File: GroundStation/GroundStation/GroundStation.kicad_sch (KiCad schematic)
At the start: 26 parts, among them J1 SD_Card_Receptacle, P1 USB_C_Plug_USB2.0, U1 STM32F103C8Tx, U4 NEO-M9N

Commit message: add little
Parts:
- renumbered R1_down to R1_up
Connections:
- net 3v3: now also R1_up.1
- net GND: no longer R1_up.2
- net USART1_GPS_EXT: now reaches U1.45 (PB8)
- net PB11_MCU_DOut: now reaches U4.8 (~{RESET})
- net PB10_DigitalOutput_whenHigh_ChipWork: no longer names the net of U4.2 (D_SEL)
- net PB10_DigitalOutput_whenHigh_ChipWork: now also R1_up.2; no longer R1_up.1
- net USART1_GPS_D_SEL renamed USART1_GPS_RESET
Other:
- note added: "Let GPS always work"
- note added: "high-gain Antenna + auto tracking 920HZ"
- note added: "low-gain Omni Antenna 433HZ"
- moved on the sheet: AE1, AE2, C1, C10, C3, C4, C5, C6, C7, C8, C9, D1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

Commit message: GPS_Ground Revise
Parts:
- added C39: 10u, symbol Device:C
- added C40: 100n, symbol Device:C
- added C41: NC, symbol Device:C
- added C42: 100p, symbol Device:C
- added D4: GPS_LED, symbol Device:LED
- added J4: Conn_Coaxial, symbol Connector:Conn_Coaxial
- added L2: short, symbol Device:L
- added R26: 1k, symbol Device:R
- added R27: NC, symbol Device:R
- added R29: 10k, symbol Device:R
- added TP1: GPS_BOOT, symbol Connector:TestPoint
- added U9: NEO-M9N-00B, SMT_9N-00B_UBL, symbol A_library:NEO-M9N-00B
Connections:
- net I_dont_know_if _it_CS?PA8 is gone; now on net SPI1_LoRa2_SCK: UE80-900M2213S.p6 (NSS)
- net PA11_USB_DX is gone; now on net USB_DX_D-: P1.A7 (D-)
- net PA12_USB_DP is gone; now on net USB_DP_D+: P1.A6 (D+)
- net PA2_TX_MCU is gone; now on net VCC: U2. (M1)
- net PA3_RX_MCU is gone; now on net VCC: U2. (M1)
- net PA4 is gone; now on net VCC: U2. (M1)
- net PA5 is gone; now on net SPI1_LoRa2_SCK: UE80-900M2213S.p6 (NSS)
- net PA6 is gone; now on net SPI1_LoRa2_MISO: UE80-900M2213S.p3 (MISO)
- net PA7 is gone; now on net SPI1_LoRa2_MOSI: UE80-900M2213S.p4 (MOSI)
- net PB1 is gone; now on net VCC: U2. (M1)
- net PB10_CS is gone; now on net SPI2_SDcard_CS: J1.1 (CD/DAT3), R2_up.2
- net PB13_SCK is gone; now on net SPI2_SDcard_MOSI: J1.5 (CLK)
- net PB14_MISO is gone; now on net SPI2_SDcard_MISO: J1.7 (DAT0)
- net PB15_MOSI is gone; now on net SPI2_SDcard_SCK: J1.2 (CMD)
- net PB2 is gone; now on net VCC: U2. (M1)
- net +3.3V: now also C39.1, C40.1, R29.1, U9.22 (V_BCKP), U9.23 (VCC)
- net GND: now also C39.2, C40.2, C41.2, D4.1 (K), J4.2 (Ext), U9.10 (GND), U9.12 (GND), U9.13 (GND), U9.24 (GND)
- net SPI1_LoRa2_CS: now also UE80-900M2213S.p6 (NSS)
- net USART1_GPS_RESET: now also R29.2, U9.8 (RESET_N)
- net USART1_GPS_RX: now also U9.20 (TXD_/_SPI_MISO)
- net USART1_GPS_TX: now also U9.21 (RXD_/_SPI_MOSI)
- net USART2_LoRa1_AUX: now also U2. (M1)
- net USART2_LoRa1_M0: now also U2. (M1)
- net USART2_LoRa1_M1: now also U2. (M1)
- net USART2_LoRa1_NRST: now also C5.1, R3_up.2, U2. (M1)
- net USART2_LoRa1_RX: now also U2. (M1)
- net USART2_LoRa1_TX: now also U2. (M1)
- removed net PB0: C5.1, R3_up.2, U2. (M1)
- net USART1_GPS_EXT: no longer names the net of U1.45 (PB8)
- new net: C41.1, C42.1, L2.2, R27.1
- new net: J4.1 (In), L2.1
- new net: D4.2 (A), R26.1
- new net: C42.2, U9.11 (RF_IN)
- new net: TP1.1, U9.1 (SAFEBOOT_N)
- new net: R26.2, U9.3 (TIMEPULSE)
- new net: R27.2, U9.9 (VCC_RF)
- no-connect marks 5 -> 16
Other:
- note added: "MCU的TX跟RX"
- note added: "Reserved for active atenna"
- moved on the sheet: AE1, AE2, C1, C10, C3, C4, C5, C6, C7, C8, C9, D1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

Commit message: Ray start GroundStation PCB
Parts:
- removed C1: 0.1uF, symbol Device:C
- removed R1_up: 10k, symbol Device:R
- removed U4: NEO-M9N, RF_GPS:ublox_NEO, symbol RF_GPS:NEO-M9N
- added C21, C23: 100n, Capacitor_SMD:C_0805_2012Metric_Pad1.18x1.45mm_HandSolder, symbol Device:C
- added C22, C24: 47u, Capacitor_SMD:C_0805_2012Metric_Pad1.18x1.45mm_HandSolder, symbol Device:C
- added D2: G_5V, LED_SMD:LED_0805_2012Metric_Pad1.15x1.40mm_HandSolder, symbol Device:LED
- added D3: B_3V3, LED_SMD:LED_0805_2012Metric_Pad1.15x1.40mm_HandSolder, symbol Device:LED
- added R16, R17: 1k, Resistor_SMD:R_0805_2012Metric, symbol Device:R
- added U3: LD1117S33TR_SOT223, Package_TO_SOT_SMD:SOT-223-3_TabPin2, symbol Regulator_Linear:LD1117S33TR_SOT223
- AE1, AE2: footprint (none) -> Connector_Coaxial:SMA_Molex_73251-1153_EdgeMount_Horizontal
- C10, C2, C3, C39, C4, C40, C41, C42, C5, C6, C7, C8, C9: footprint (none) -> Capacitor_SMD:C_0805_2012Metric_Pad1.18x1.45mm_HandSolder
- C66: renamed from C6; footprint (none) -> Capacitor_SMD:C_0805_2012Metric_Pad1.18x1.45mm_HandSolder
- C77: renamed from C7; footprint (none) -> Capacitor_SMD:C_0805_2012Metric_Pad1.18x1.45mm_HandSolder
- D4: footprint (none) -> LED_SMD:LED_0805_2012Metric_Pad1.15x1.40mm_HandSolder
- FB1: footprint (none) -> Inductor_SMD:L_2512_6332Metric
- J1: footprint (none) -> Connector_Card:SD_Kyocera_145638109511859+
- J4: footprint (none) -> Connector_Coaxial:BNC_Amphenol_B6252HB-NPP3G-50_Horizontal
- L2: footprint (none) -> Inductor_SMD:L_Bourns_SDR0604
- P1: footprint (none) -> Connector_USB:USB3_A_Molex_48393-001
- R26, R27, R29, R3_up1: footprint (none) -> Resistor_SMD:R_0805_2012Metric
- R2_up1: renamed from R2_up; footprint (none) -> Resistor_SMD:R_0805_2012Metric
- R3_up2: renamed from R3_up; footprint (none) -> Resistor_SMD:R_0805_2012Metric
- TP1: footprint (none) -> TestPoint:TestPoint_Pad_D1.0mm
- U2: value ~ -> E22-400T30S_LoRa
- U9: footprint SMT_9N-00B_UBL -> RF_GPS:ublox_NEO
- renumbered UE80-900M2213S to UE80-900M2213S1
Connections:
- net 3v3 is gone; now on net 3.3V: C2.1, J1.4 (VDD), R2_up1.1
- net +5V: now also C23.1, R16.2, U3.3 (VI)
- net GND: now also C21.2, C22.2, C23.2, C24.2, D2.1 (K), D3.1 (K), U3.1 (GND)
- net SPI1_LoRa2_CS: now also UE80-900M2213S1.p7 (NSS); no longer UE80-900M2213S1.p6 (NSS)
- net +3.3V renamed 3.3V
- net 3.3V: now also C3.1, C4.1, R3_up2.1, U2. (M1), C21.1, C22.1, C24.1, R17.2, U3.2 (VO)
- removed net VCC: C3.1, C4.1, R3_up2.1, U2. (M1)
- new net: D2.2 (A), R16.1
- new net: D3.2 (A), R17.1
- no-connect marks 16 -> 41
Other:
- note added: "Indicator"
- note added: "LDO"
- note removed: "Let GPS always work"
- moved on the sheet: C10, C6, C66, C7, C77, C8, C9, FB1, TP1, U1

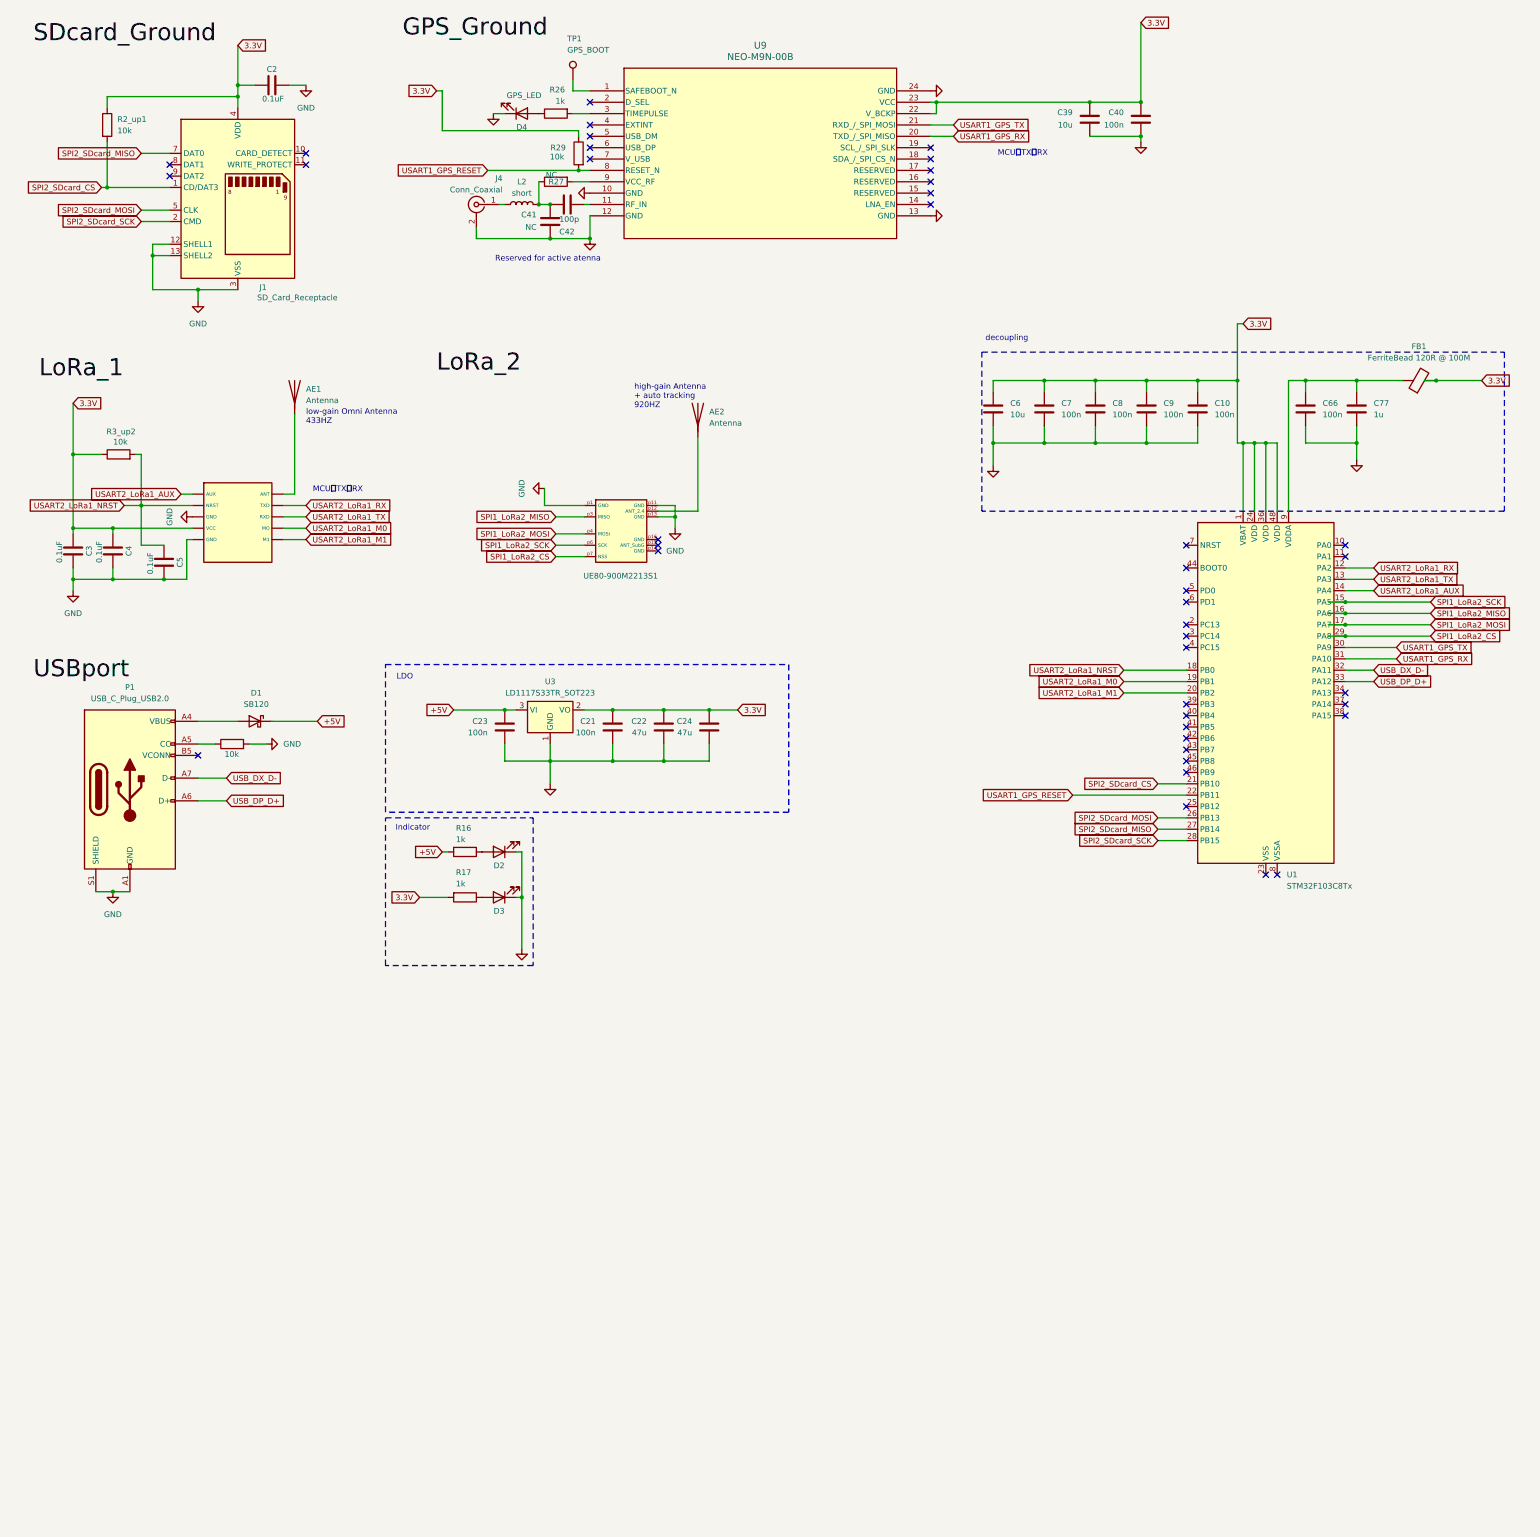
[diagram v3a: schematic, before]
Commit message: assign package for groundstation
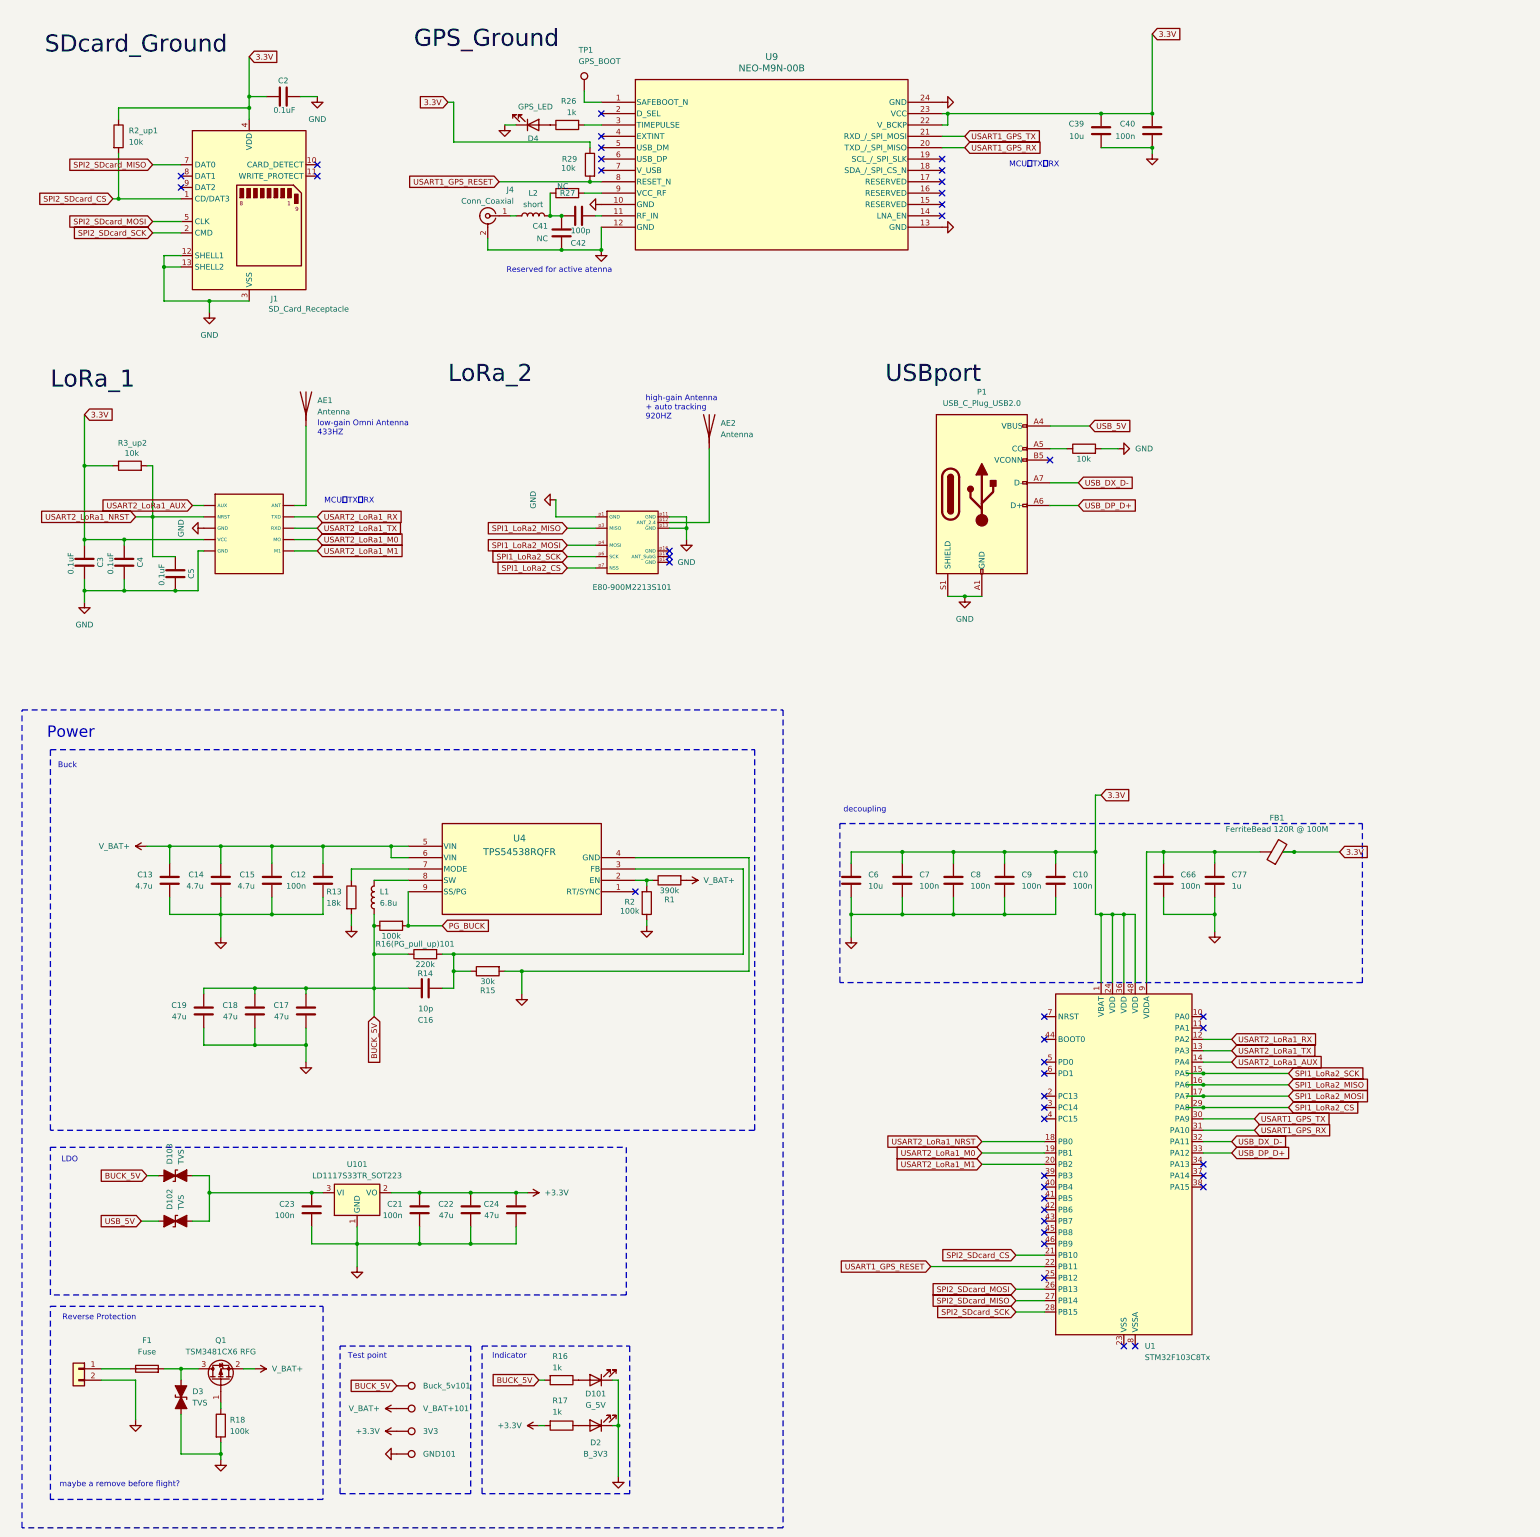
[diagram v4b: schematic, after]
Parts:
- removed D1: SB120, Diode_THT:D_DO-41_SOD81_P10.16mm_Horizontal, symbol Diode:SB120
- removed D2: G_5V, LED_SMD:LED_0805_2012Metric_Pad1.15x1.40mm_HandSolder, symbol Device:LED
- removed U3: LD1117S33TR_SOT223, Package_TO_SOT_SMD:SOT-223-3_TabPin2, symbol Regulator_Linear:LD1117S33TR_SOT223
- added 3V3, Buck_5v101, GND101, V_BAT+101: TestPoint, TestPoint:TestPoint_Pad_2.0x2.0mm, symbol Connector:TestPoint
- added C12: 100n, Capacitor_SMD:C_0805_2012Metric_Pad1.18x1.45mm_HandSolder, symbol Device:C
- added C13, C14, C15: 4.7u, Capacitor_SMD:C_0805_2012Metric_Pad1.18x1.45mm_HandSolder, symbol Device:C
- added C16: 10p, Capacitor_SMD:C_0805_2012Metric_Pad1.18x1.45mm_HandSolder, symbol Device:C
- added C17, C18, C19: 47u, Capacitor_SMD:C_0805_2012Metric_Pad1.18x1.45mm_HandSolder, symbol Device:C
- added D101: G_5V, LED_SMD:LED_0805_2012Metric_Pad1.15x1.40mm_HandSolder, symbol Device:LED
- added D102, D103, D3: TVS, Diode_SMD:D_SOD-123, symbol Device:D_TVS_Filled
- added F1: Fuse, Fuse:Fuse_1206_3216Metric, symbol Device:Fuse
- added J5: Conn_01x02, Connector_PinHeader_2.54mm:PinHeader_1x02_P2.54mm_Horizontal, symbol Connector_Generic:Conn_01x02
- added L1: 6.8u, Inductor_SMD:L_0805_2012Metric_Pad1.05x1.20mm_HandSolder, symbol Device:L
- added Q1: TSM3481CX6 RFG, Package_TO_SOT_SMD:SOT-23, symbol Transistor_FET:IRLML6402
- added R1: 390k, Resistor_SMD:R_0805_2012Metric_Pad1.20x1.40mm_HandSolder, symbol Device:R
- added R13: 18k, Resistor_SMD:R_0805_2012Metric_Pad1.20x1.40mm_HandSolder, symbol Device:R
- added R14: 220k, Resistor_SMD:R_0805_2012Metric_Pad1.20x1.40mm_HandSolder, symbol Device:R
- added R15: 30k, Resistor_SMD:R_0805_2012Metric_Pad1.20x1.40mm_HandSolder, symbol Device:R
- added R16(PG_pull_up)101, R18, R2: 100k, Resistor_SMD:R_0805_2012Metric_Pad1.20x1.40mm_HandSolder, symbol Device:R
- added U101: LD1117S33TR_SOT223, Package_TO_SOT_SMD:SOT-223-3_TabPin2, symbol Regulator_Linear:LD1117S33TR_SOT223
- added U4: TPS54538RQFR, RF:TPS54538RQFR, symbol Small_av_tony_lib:TPS54538RQFR
- E80-900M2213S101: renamed from UE80-900M2213S1; footprint (none) -> RF:E80-900M2213S
- R16, R17, R26, R27, R29, R2_up1, R3_up1, R3_up2: footprint Resistor_SMD:R_0805_2012Metric -> Resistor_SMD:R_0805_2012Metric_Pad1.20x1.40mm_HandSolder
- U2: footprint (none) -> Library:e22-400t30s_Package
- renumbered D3 to D2
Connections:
- net 3.3V: no longer C21.1, C22.1, C24.1, R17.2
- net GND: now also C12.2, C13.2, C14.2, C15.2, C17.2, C18.2, C19.2, D101.1 (K), D3.1 (A1), GND101.1, J5.2 (Pin_2), R13.2, R15.2, R18.2, R2.1, U101.1 (GND), U4.4 (GND)
- net USB_5V: now reaches P1.A4 (VBUS), P1.A9 (VBUS), P1.B4 (VBUS), P1.B9 (VBUS)
- net USB_5V: now also D102.2 (A2)
- net at R16.1: now also D101.2 (A)
- net +5V: no longer names the net of C23.1
- net +5V: now also D102.1 (A1), D103.1 (A1), U101.3 (VI); no longer R16.2
- new net: C16.2, R14.2, R15.1, U4.3 (FB)
- new net: F1.1, J5.1 (Pin_1)
- new net: D3.2 (A2), F1.2, Q1.3 (D)
- new net: R1.1, R2.2, U4.2 (EN)
- new net: L1.2, U4.8 (SW)
- new net: R13.1, U4.7 (MODE)
- new net: Q1.1 (G), R18.1
- new net +3.3V: 3V3.1, C21.1, C22.1, C24.1, R17.2, U101.2 (VO)
- new net BUCK_5V: Buck_5v101.1, C16.1, C17.1, C18.1, C19.1, D103.2 (A2), L1.1, R14.1, R16(PG_pull_up)101.1, R16.2
- new net PG_BUCK: R16(PG_pull_up)101.2, U4.9 (SS/PG)
- new net V_BAT+: C12.1, C13.1, C14.1, C15.1, Q1.2 (S), R1.2, U4.5 (VIN), U4.6 (VIN), V_BAT+101.1
- no-connect marks 41 -> 42
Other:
- note added: "Buck"
- note added: "Power"
- note added: "Reverse Protection"
- note added: "Test point"
- note added: "maybe a remove before flight?"
- moved on the sheet: AE1, AE2, C10, C2, C21, C22, C23, C24, C3, C39, C4, C40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
